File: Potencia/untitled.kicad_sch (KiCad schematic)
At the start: 13 parts, among them U3.3 LM2596S-3.3, U5 LM2596S-5

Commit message: se añade relé, se corrigen parámetros
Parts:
- added D?: Led_ON, LED_SMD:LED_0603_1608Metric_Pad1.05x0.95mm_HandSolder, symbol LED:IR26-21C_L110_TR8
- added R?: 68, Resistor_SMD:R_1206_3216Metric_Pad1.30x1.75mm_HandSolder, symbol Device:R
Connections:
- net +3.3V: now also R?.1
- net GND: now also D?.1 (K)
- new net: D?.2 (A), R?.2
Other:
- note added: "Led de encendido"

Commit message: guardado
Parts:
- gave numbers to parts that had none: 3
- renumbered CIn0 to CIn1, CIn2 to CIn3, Cin1 to Cin2, D1 to D4, D2 to D5, DIn to DIn1, U5 to U3, U3.3 to U3.1

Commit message: dddd
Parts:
- removed D6: Led_ON, LED_SMD:LED_0603_1608Metric_Pad1.05x0.95mm_HandSolder, symbol LED:IR26-21C_L110_TR8
- removed R9: 68, Resistor_SMD:R_1206_3216Metric_Pad1.30x1.75mm_HandSolder, symbol Device:R
- added CIn? (x2): (no value), symbol Device:C
- added U?: (no value), symbol Regulator_Linear:LM7912_TO220
- CIn0: renamed from CIn1; value 22uF -> (none); footprint Capacitor_SMD:C_0805_2012Metric_Pad1.18x1.45mm_HandSolder -> (none)
- CIn2: renamed from CIn3; value 680u -> (none)
- COut1, COut2: value 220u -> (none)
- Cin1: renamed from Cin2; value 680u -> (none)
- D1: renamed from D4; value 1N5822 -> (none); footprint Diode_THT:D_DO-201AD_P15.24mm_Horizontal -> (none)
- D2: renamed from D5; value 1N5822 -> (none); footprint Diode_THT:D_DO-201AD_P15.24mm_Horizontal -> (none)
- DIn: renamed from DIn1; value 1N4007 -> (none); footprint Diode_SMD:D_SMA_Handsoldering -> (none)
- JP?: renamed from JP1; value Jumper_3_Open -> (none); footprint Connector_PinHeader_2.54mm:PinHeader_1x03_P2.54mm_Vertical -> (none)
- L1, L2: value 33u -> (none)
- U3.3: renamed from U3.1; value LM2596S-3.3 -> (none); footprint Package_TO_SOT_SMD:TO-263-5_TabPin3 -> (none)
- U5: renamed from U3; value LM2596S-5 -> (none); footprint Package_TO_SOT_SMD:TO-263-5_TabPin3 -> (none)
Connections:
- net GND: now also CIn?.1, CIn?.1, U?.1 (GND)
- new net: CIn?.2, U?.3 (VO)
- new net: CIn?.2, U?.2 (VI)
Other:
- note removed: "Led de encendido"

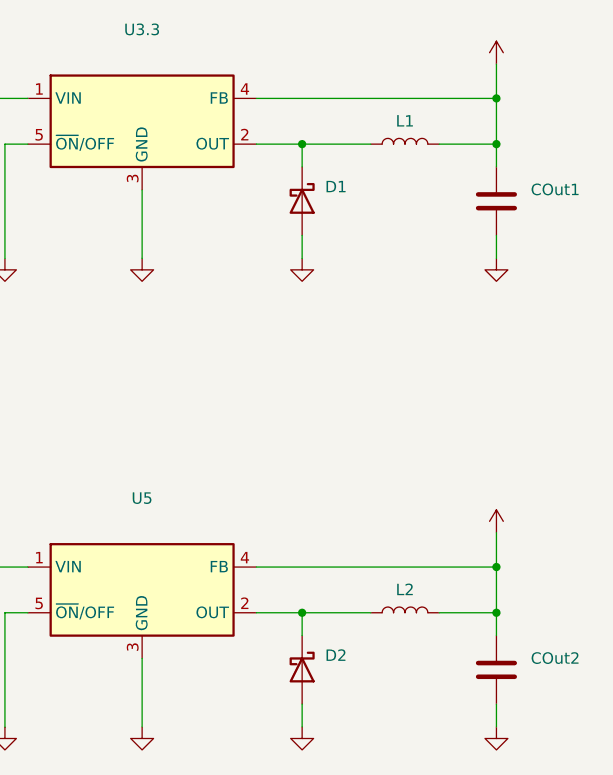
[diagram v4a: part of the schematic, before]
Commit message: Cambio de pantalla
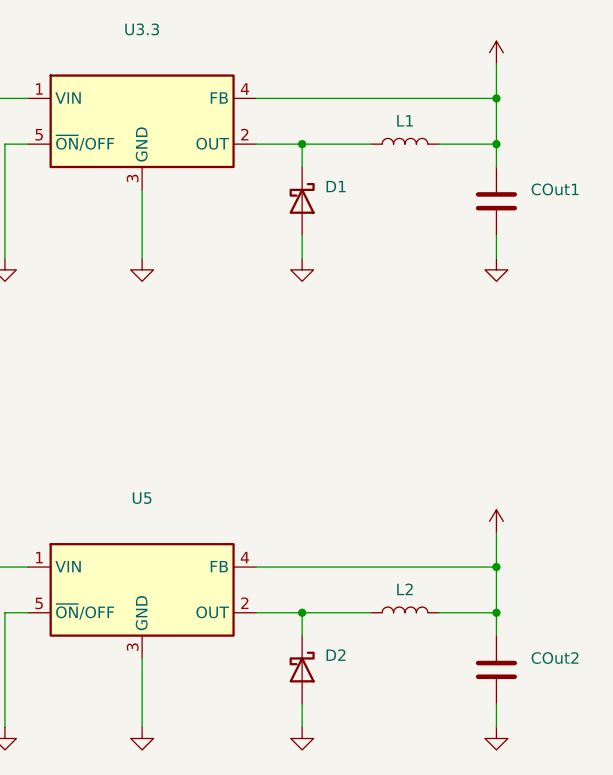
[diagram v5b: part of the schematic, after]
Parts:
- CIn0, CIn2, CIn? (x2), COut1, COut2, Cin1, D1, D2, DIn, JP?, L1, L2, U3.3, U5, U?: value (none) -> ~
